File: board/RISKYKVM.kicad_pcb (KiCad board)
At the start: 4 copper layers, 24.9 x 35.6 mm, 19 parts, among them J1 DE9_Plug, J2 Conn_01x02, J3 USB_1, J4 Conn_01x08, U1 CH32V203C8T6, U2 LM1117MP-3.3

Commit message: v0.2
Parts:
- moved R3 2.02 mm to (119.8, 78.2), turned to 90 degrees
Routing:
- net +3.3V: track 50.5 -> 23.0 mm, vias 8 -> 7
- net GND: vias 12 -> 11
- added copper zone on In2.Cu, net +3.3V
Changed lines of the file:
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@@
     (fp_line (start 1 0.6) (end 1 -0.6)
       (stroke (width 0.1) (type solid)) (layer "F.Fab"))
-    (pad "1" smd roundrect (at -1.025 0 90) (size 1.15 1.4) (layers "F.Cu" "F.Paste" "F.Mask") (roundrect_rratio 0.217391)
+    (pad "1" smd roundrect (at -1.025 0 90) (size 1.15 1.4) (layers "F.Cu" "F.Paste" "F.Mask") (roundrect_rratio 0.2173913043)
       (net 44 "/LED1") (pinfunction "K") (pintype "passive"))
-    (pad "2" smd roundrect (at 1.025 0 90) (size 1.15 1.4) (layers "F.Cu" "F.Paste" "F.Mask") (roundrect_rratio 0.217391)
+    (pad "2" smd roundrect (at 1.025 0 90) (size 1.15 1.4) (layers "F.Cu" "F.Paste" "F.Mask") (roundrect_rratio 0.2173913043)
       (net 45 "Net-(D2-A)") (pinfunction "A") (pintype "passive"))
     (model "${KICAD6_3DMODEL_DIR}/LED_SMD.3dshapes/LED_0805_2012Metric.wrl"
@@
     (fp_line (start 1 0.6) (end 1 -0.6)
       (stroke (width 0.1) (type solid)) (layer "F.Fab"))
-    (pad "1" smd roundrect (at -1.025 0 90) (size 1.15 1.4) (layers "F.Cu" "F.Paste" "F.Mask") (roundrect_rratio 0.217391)
+    (pad "1" smd roundrect (at -1.025 0 90) (size 1.15 1.4) (layers "F.Cu" "F.Paste" "F.Mask") (roundrect_rratio 0.2173913043)
       (net 2 "GND") (pinfunction "K") (pintype "passive"))
-    (pad "2" smd roundrect (at 1.025 0 90) (size 1.15 1.4) (layers "F.Cu" "F.Paste" "F.Mask") (roundrect_rratio 0.217391)
+    (pad "2" smd roundrect (at 1.025 0 90) (size 1.15 1.4) (layers "F.Cu" "F.Paste" "F.Mask") (roundrect_rratio 0.2173913043)
       (net 18 "Net-(D1-A)") (pinfunction "A") (pintype "passive"))
     (model "${KICAD6_3DMODEL_DIR}/LED_SMD.3dshapes/LED_0805_2012Metric.wrl"
@@
   )
   (footprint "Resistor_SMD:R_0603_1608Metric_Pad0.98x0.95mm_HandSolder" (layer "B.Cu")
-    (at 119.8 80.27 -90)
+    (at 119.775 78.25 90)
     (descr "Resistor SMD 0603 (1608 Metric), square (rectangular) end terminal, IPC_7351 nominal with elongated pad for handsoldering. (Body size source: IPC-SM-782 page 72, https://www.pcb-3d.com/wordpress/wp-content/uploads/ipc-sm-782a_amendment_1_and_2.pdf), generated with kicad-footprint-generator")
     (tags "resistor handsolder")
@@
     (property "ki_keywords" "R res resistor")
     (attr smd)
-    (fp_text reference "R3" (at 2.93 -0.1 90) (layer "B.SilkS")
+    (fp_text reference "R3" (at -2.8 0.125 270) (layer "B.SilkS")
         (effects (font (size 1 1) (thickness 0.15)) (justify mirror))
     )
@@
     (fp_line (start 0.8 0.4125) (end 0.8 -0.4125)
       (stroke (width 0.1) (type solid)) (layer "B.Fab"))
-    (pad "1" smd roundrect (at -0.9125 0 270) (size 0.975 0.95) (layers "B.Cu" "B.Paste" "B.Mask") (roundrect_rratio 0.25)
+    (pad "1" smd roundrect (at -0.9125 0 90) (size 0.975 0.95) (layers "B.Cu" "B.Paste" "B.Mask") (roundrect_rratio 0.25)
       (net 45 "Net-(D2-A)") (pintype "passive"))
-    (pad "2" smd roundrect (at 0.9125 0 270) (size 0.975 0.95) (layers "B.Cu" "B.Paste" "B.Mask") (roundrect_rratio 0.25)
+    (pad "2" smd roundrect (at 0.9125 0 90) (size 0.975 0.95) (layers "B.Cu" "B.Paste" "B.Mask") (roundrect_rratio 0.25)
       (net 1 "+3.3V") (pintype "passive"))
     (model "${KICAD6_3DMODEL_DIR}/Resistor_SMD.3dshapes/R_0603_1608Metric.wrl"
@@
     (property "ki_keywords" "R res resistor")
     (attr smd)
-    (fp_text reference "R2" (at 0.0762 -1.27 270) (layer "B.SilkS")
+    (fp_text reference "R2" (at 0.1078 -1.7122 270) (layer "B.SilkS")
         (effects (font (size 1 1) (thickness 0.15)) (justify mirror))
     )
@@
     (effects (font (size 0.8128 0.8128) (thickness 0.1524) bold) (justify left bottom))
   )
-  (gr_text "POWER" (at 122.5 108.2 90) (layer "F.SilkS")
+  (gr_text "POWER" (at 123.15 108.125 90) (layer "F.SilkS")
     (effects (font (size 0.8128 0.8128) (thickness 0.1524) bold) (justify left bottom))
   )
@@
   (segment (start 125.596121 93.916221) (end 125.5861 93.9062) (width 0.127) (layer "F.Cu") (net 1))
   (segment (start 126.9986 90.0146) (end 126.9986 90.2364) (width 0.2) (layer "F.Cu") (net 1))
-  (segment (start 132.0854 95.4502) (end 132.4664 95.8312) (width 0.2) (layer "F.Cu") (net 1))
   (segment (start 132.4986 96.8187) (end 132.4997 96.8198) (width 0.127) (layer "F.Cu") (net 1))
   (segment (start 126.9986 88.4937) (end 126.9986 90.0146) (width 0.2) (layer "F.Cu") (net 1))
@@
   (segment (start 126.9986 90.2364) (end 127.107 90.3448) (width 0.2) (layer "F.Cu") (net 1))
   (segment (start 125.5861 89.9062) (end 126.8902 89.9062) (width 0.2) (layer "F.Cu") (net 1))
-  (segment (start 123.87 86.83) (end 123.87 86.82) (width 0.127) (layer "F.Cu") (net 1))
   (segment (start 133.9111 89.9062) (end 132.4986 89.9062) (width 0.2) (layer "F.Cu") (net 1))
   (segment (start 132.4664 96.7865) (end 132.4986 96.8187) (width 0.127) (layer "F.Cu") (net 1))
-  (segment (start 132.0854 90.3194) (end 127.1324 90.3194) (width 0.2) (layer "F.Cu") (net 1))
-  (segment (start 132.0854 90.3194) (end 132.0854 95.4502) (width 0.2) (layer "F.Cu") (net 1))
-  (segment (start 125.41 88.37) (end 123.87 86.83) (width 0.127) (layer "F.Cu") (net 1))
   (segment (start 132.4664 95.8312) (end 132.4664 96.7865) (width 0.127) (layer "F.Cu") (net 1))
-  (via (at 125.41 88.37) (size 0.6) (drill 0.3) (layers "F.Cu" "B.Cu") (net 1))
-  (via (at 123.87 86.82) (size 0.6) (drill 0.3) (layers "F.Cu" "B.Cu") (net 1))
   (via (at 122.63 98.74) (size 0.6) (drill 0.3) (layers "F.Cu" "B.Cu") (net 1))
   (via (at 132.0854 90.3194) (size 0.6) (drill 0.3) (layers "F.Cu" "B.Cu") (net 1))
+  (via (at 119.775 77.375) (size 0.6) (drill 0.3) (layers "F.Cu" "B.Cu") (net 1))
   (via (at 132.4664 95.8312) (size 0.6) (drill 0.3) (layers "F.Cu" "B.Cu") (net 1))
-  (via (at 122.63 100.1935) (size 0.6) (drill 0.3) (layers "F.Cu" "B.Cu") (net 1))
+  (via (at 121.925 104.65) (size 0.6) (drill 0.3) (layers "F.Cu" "B.Cu") (net 1))
   (via (at 127.107 90.3448) (size 0.6) (drill 0.3) (layers "F.Cu" "B.Cu") (net 1))
   (via (at 126.530218 93.916221) (size 0.6) (drill 0.3) (layers "F.Cu" "B.Cu") (net 1))
@@
   (segment (start 126.530218 94.264918) (end 126.530218 93.916221) (width 0.127) (layer "B.Cu") (net 1))
   (segment (start 127.5134 95.2481) (end 126.530218 94.264918) (width 0.127) (layer "B.Cu") (net 1))
-  (segment (start 121.905 103.955) (end 122.64 103.22) (width 0.127) (layer "B.Cu") (net 1))
   (segment (start 127.8222 95.5569) (end 131.7744 95.5569) (width 0.127) (layer "B.Cu") (net 1))
   (segment (start 122.5834 98.6934) (end 122.63 98.74) (width 0.127) (layer "B.Cu") (net 1))
   (segment (start 126.776139 93.6703) (end 126.530218 93.916221) (width 0.127) (layer "B.Cu") (net 1))
   (segment (start 132.4399 95.8047) (end 132.4664 95.8312) (width 0.2) (layer "B.Cu") (net 1))
-  (segment (start 121.905 104.72) (end 121.905 103.955) (width 0.127) (layer "B.Cu") (net 1))
   (segment (start 126.1219 95.2481) (end 122.63 98.74) (width 0.127) (layer "B.Cu") (net 1))
-  (segment (start 127.2097 90.1697) (end 125.41 88.37) (width 0.127) (layer "B.Cu") (net 1))
   (segment (start 127.4372 93.6703) (end 126.776139 93.6703) (width 0.127) (layer "B.Cu") (net 1))
-  (segment (start 122.64 100.2035) (end 122.63 100.1935) (width 0.127) (layer "B.Cu") (net 1))
   (segment (start 127.1589 90.3448) (end 127.2097 90.294) (width 0.2) (layer "B.Cu") (net 1))
-  (segment (start 122.64 103.22) (end 122.64 100.2035) (width 0.127) (layer "B.Cu") (net 1))
   (segment (start 127.5134 95.2481) (end 127.8222 95.5569) (width 0.127) (layer "B.Cu") (net 1))
   (segment (start 131.7744 95.5569) (end 132.4399 94.8914) (width 0.127) (layer "B.Cu") (net 1))
   (segment (start 127.107 90.3448) (end 127.1589 90.3448) (width 0.2) (layer "B.Cu") (net 1))
-  (segment (start 123.87 85.2525) (end 119.8 81.1825) (width 0.127) (layer "B.Cu") (net 1))
-  (segment (start 123.87 86.82) (end 123.87 85.2525) (width 0.127) (layer "B.Cu") (net 1))
   (segment (start 127.5134 95.2481) (end 126.1219 95.2481) (width 0.127) (layer "B.Cu") (net 1))
   (segment (start 127.2097 90.294) (end 127.2097 90.1697) (width 0.127) (layer "B.Cu") (net 1))
@@
   (via (at 129.72 77.77) (size 0.6) (drill 0.3) (layers "F.Cu" "B.Cu") (free) (net 2))
   (via (at 128.01 99.54) (size 0.6) (drill 0.3) (layers "F.Cu" "B.Cu") (free) (net 2))
-  (via (at 121.95 85.32) (size 0.6) (drill 0.3) (layers "F.Cu" "B.Cu") (free) (net 2))
   (via (at 127.5 87.39) (size 0.6) (drill 0.3) (layers "F.Cu" "B.Cu") (net 2))
   (via (at 122.6 97) (size 0.6) (drill 0.3) (layers "F.Cu" "B.Cu") (net 2))
@@
       )
     )
+  )
+  (zone (net 1) (net_name "+3.3V") (layer "In2.Cu") (hatch edge 0.5)
+    (priority 4)
+    (connect_pads (clearance 0.5))
+    (min_thickness 0.25) (filled_areas_thickness no)
+    (fill yes (thermal_gap 0.5) (thermal_bridge_width 0.5))
+    (polygon
+      (pts
+        (xy 142.9 74.85)
+        (xy 142.9 110.35)
+        (xy 118.025 110.35)
+        (xy 118 74.85)
+      )
+    )

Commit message: Fix issues related to BOOT0 and BOOT1
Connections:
- U1 pad 20: /PIN5 -> GND
- U1 pad 21: /PIN9 -> /PIN5
- U1 pad 22: /PIN4 -> /PIN9
- U1 pad 25: /PIN3 -> /PIN4
- U1 pad 26: /PIN2 -> /PIN3
- U1 pad 27: /PIN6 -> /PIN2
- U1 pad 28: /PIN1 -> /PIN6
- U1 pad 29: unconnected-(U1-PA8(FT)-Pad29) -> /PIN1
- U1 pad 44: unconnected-(U1-BOOT0-Pad44) -> GND
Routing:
- net GND: track 16.6 -> 21.4 mm, vias 11 -> 10
- net /PIN4: track 12.6 -> 15.3 mm
- net /PIN3: track 13.9 -> 15.9 mm
- net /PIN5: track 13.4 -> 14.4 mm
- net /PIN2: track 14.4 -> 15.5 mm
- net /PIN6: track 14.7 -> 15.6 mm
- net /PIN1: track 15.1 -> 15.9 mm
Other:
- board text added: "5V"
- board text added: "CL"
- board text added: "DT"
- board text added: "G"
- board text added: "PWR"
- board text added: "R"
- board text added: "RDY"
- board text removed: "POWER"
- board text removed: "READY"

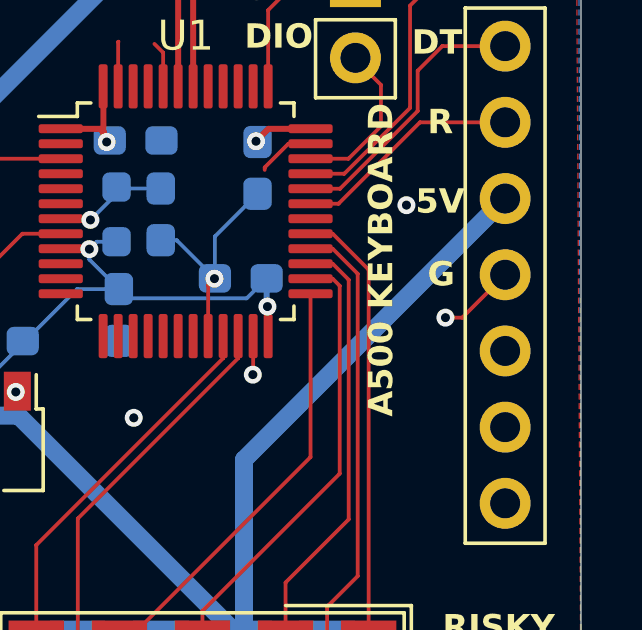
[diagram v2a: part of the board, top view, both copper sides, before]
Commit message: KEY in Amiga Port missing
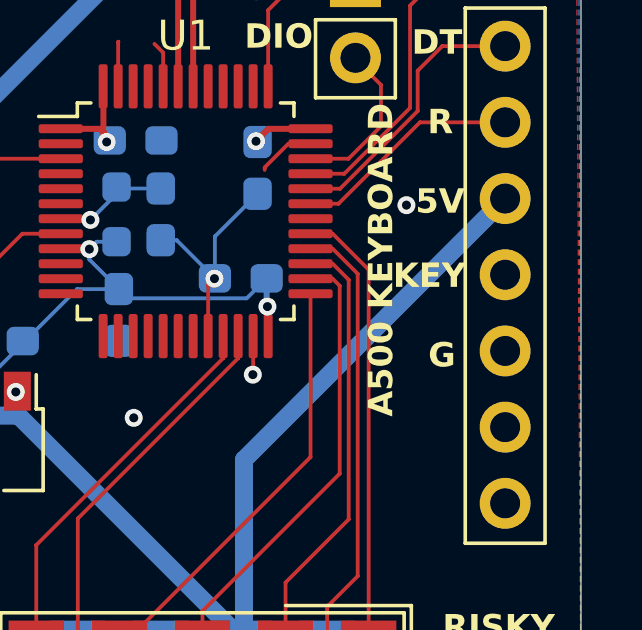
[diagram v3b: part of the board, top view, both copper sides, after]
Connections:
- J4 pad 5: GND -> unconnected-(J4-Pin_5-Pad5)
- J4 pad 6: unconnected-(J4-Pin_6-Pad6) -> GND
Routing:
- net GND: track 21.4 -> 18.8 mm, vias 10 -> 9
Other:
- board text added: "KEY"
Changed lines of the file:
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@@
   (net 21 "unconnected-(U1-PB0_ADC8-Pad18)")
   (net 22 "unconnected-(U1-PB1_ADC9-Pad19)")
-  (net 23 "/KB_CLK")
-  (net 24 "/KB_DATA")
-  (net 25 "/KB_RESET")
-  (net 26 "unconnected-(J4-Pin_6-Pad6)")
+  (net 23 "unconnected-(J4-Pin_5-Pad5)")
+  (net 24 "/KB_CLK")
+  (net 25 "/KB_DATA")
+  (net 26 "/KB_RESET")
   (net 27 "unconnected-(J4-Pin_7-Pad7)")
   (net 28 "unconnected-(J4-Pin_8-Pad8)")
@@
       (stroke (width 0.1) (type solid)) (layer "F.Fab"))
     (pad "1" thru_hole rect (at 0 0) (size 1.7 1.7) (drill 1) (layers "*.Cu" "*.Mask")
-      (net 23 "/KB_CLK") (pinfunction "Pin_1") (pintype "passive"))
+      (net 24 "/KB_CLK") (pinfunction "Pin_1") (pintype "passive"))
     (pad "2" thru_hole oval (at 0 2.54) (size 1.7 1.7) (drill 1) (layers "*.Cu" "*.Mask")
-      (net 24 "/KB_DATA") (pinfunction "Pin_2") (pintype "passive"))
+      (net 25 "/KB_DATA") (pinfunction "Pin_2") (pintype "passive"))
     (pad "3" thru_hole oval (at 0 5.08) (size 1.7 1.7) (drill 1) (layers "*.Cu" "*.Mask")
-      (net 25 "/KB_RESET") (pinfunction "Pin_3") (pintype "passive"))
+      (net 26 "/KB_RESET") (pinfunction "Pin_3") (pintype "passive"))
     (pad "4" thru_hole oval (at 0 7.62) (size 1.7 1.7) (drill 1) (layers "*.Cu" "*.Mask")
       (net 3 "+5V") (pinfunction "Pin_4") (pintype "passive"))
     (pad "5" thru_hole oval (at 0 10.16) (size 1.7 1.7) (drill 1) (layers "*.Cu" "*.Mask")
-      (net 2 "GND") (pinfunction "Pin_5") (pintype "passive"))
+      (net 23 "unconnected-(J4-Pin_5-Pad5)") (pinfunction "Pin_5") (pintype "passive+no_connect"))
     (pad "6" thru_hole oval (at 0 12.7) (size 1.7 1.7) (drill 1) (layers "*.Cu" "*.Mask")
-      (net 26 "unconnected-(J4-Pin_6-Pad6)") (pinfunction "Pin_6") (pintype "passive+no_connect"))
+      (net 2 "GND") (pinfunction "Pin_6") (pintype "passive"))
     (pad "7" thru_hole oval (at 0 15.24) (size 1.7 1.7) (drill 1) (layers "*.Cu" "*.Mask")
       (net 27 "unconnected-(J4-Pin_7-Pad7)") (pinfunction "Pin_7") (pintype "passive+no_connect"))
@@
       (net 38 "unconnected-(U1-PA9(FT)-Pad30)") (pinfunction "PA9(FT)") (pintype "bidirectional+no_connect"))
     (pad "31" smd roundrect (at 4.1625 -0.25) (size 1.475 0.3) (layers "F.Cu" "F.Paste" "F.Mask") (roundrect_rratio 0.25)
-      (net 25 "/KB_RESET") (pinfunction "PA10(FT)") (pintype "bidirectional"))
+      (net 26 "/KB_RESET") (pinfunction "PA10(FT)") (pintype "bidirectional"))
     (pad "32" smd roundrect (at 4.1625 -0.75) (size 1.475 0.3) (layers "F.Cu" "F.Paste" "F.Mask") (roundrect_rratio 0.25)
-      (net 24 "/KB_DATA") (pinfunction "PA11_USB1DM(FT)") (pintype "bidirectional"))
+      (net 25 "/KB_DATA") (pinfunction "PA11_USB1DM(FT)") (pintype "bidirectional"))
     (pad "33" smd roundrect (at 4.1625 -1.25) (size 1.475 0.3) (layers "F.Cu" "F.Paste" "F.Mask") (roundrect_rratio 0.25)
-      (net 23 "/KB_CLK") (pinfunction "PA12_USB1DP(FT)") (pintype "bidirectional"))
+      (net 24 "/KB_CLK") (pinfunction "PA12_USB1DP(FT)") (pintype "bidirectional"))
     (pad "34" smd roundrect (at 4.1625 -1.75) (size 1.475 0.3) (layers "F.Cu" "F.Paste" "F.Mask") (roundrect_rratio 0.25)
       (net 13 "/SWDIO") (pinfunction "PA13_SWDIO(FT)") (pintype "bidirectional"))
@@
     (effects (font (size 0.8128 0.8128) (thickness 0.1524) bold) (justify left bottom))
   )
-  (gr_text "G" (at 137.8 95.225) (layer "F.SilkS")
+  (gr_text "G" (at 137.825 97.925) (layer "F.SilkS")
     (effects (font (size 0.8128 0.8128) (thickness 0.1524) bold) (justify left bottom))
   )
@@
   )
   (gr_text "5V" (at 137.4 92.8) (layer "F.SilkS")
+    (effects (font (size 0.8128 0.8128) (thickness 0.1524) bold) (justify left bottom))
+  )
+  (gr_text "KEY" (at 136.65 95.275) (layer "F.SilkS")
     (effects (font (size 0.8128 0.8128) (thickness 0.1524) bold) (justify left bottom))
   )
@@
   (segment (start 130.49 95.11) (end 130.7 94.9) (width 0.127) (layer "F.Cu") (net 2))
   (segment (start 132.375 91.192501) (end 132.375 91.275) (width 0.127) (layer "F.Cu") (net 2))
-  (segment (start 138.96 96.2) (end 140.39 94.77) (width 0.127) (layer "F.Cu") (net 2))
-  (segment (start 138.4 96.2) (end 138.96 96.2) (width 0.127) (layer "F.Cu") (net 2))
   (segment (start 130.49 96.815) (end 130.49 95.11) (width 0.127) (layer "F.Cu") (net 2))
   (segment (start 127.49 87.01) (end 127.5 87) (width 0.127) (layer "F.Cu") (net 2))
@@
   (via (at 137.1 92.45) (size 0.6) (drill 0.3) (layers "F.Cu" "B.Cu") (free) (net 2))
   (via (at 128.9 108.1) (size 0.6) (drill 0.3) (layers "F.Cu" "B.Cu") (net 2))
-  (via (at 138.4 96.2) (size 0.6) (drill 0.3) (layers "F.Cu" "B.Cu") (free) (net 2))
   (via (at 131.98 98.1) (size 0.6) (drill 0.3) (layers "F.Cu" "B.Cu") (net 2))
   (via (at 124.0778 98.6769) (size 0.6) (drill 0.3) (layers "F.Cu" "B.Cu") (net 2))
@@
   (segment (start 129.5186 81.6107) (end 129.175 81.2671) (width 0.2) (layer "F.Cu") (net 16))
   (via (at 120.15 104.63) (size 0.6) (drill 0.3) (layers "F.Cu" "B.Cu") (net 18))
-  (segment (start 133.9025 91.4025) (end 135.026982 91.4025) (width 0.127) (layer "F.Cu") (net 23))
-  (segment (start 135.026982 91.4025) (end 137.22 89.209482) (width 0.127) (layer "F.Cu") (net 23))
-  (segment (start 138.41 84.61) (end 140.39 84.61) (width 0.127) (layer "F.Cu") (net 23))
-  (segment (start 137.22 85.8) (end 138.41 84.61) (width 0.127) (layer "F.Cu") (net 23))
-  (segment (start 137.22 89.209482) (end 137.22 85.8) (width 0.127) (layer "F.Cu") (net 23))
-  (segment (start 138.294 87.15) (end 140.39 87.15) (width 0.127) (layer "F.Cu") (net 24))
-  (segment (start 137.474 87.97) (end 138.294 87.15) (width 0.127) (layer "F.Cu") (net 24))
-  (segment (start 133.9025 91.9025) (end 134.886192 91.9025) (width 0.127) (layer "F.Cu") (net 24))
-  (segment (start 134.886192 91.9025) (end 137.474 89.314692) (width 0.127) (layer "F.Cu") (net 24))
-  (segment (start 137.474 89.314692) (end 137.474 87.97) (width 0.127) (layer "F.Cu") (net 24))
-  (segment (start 133.9025 92.4025) (end 134.8375 92.4025) (width 0.127) (layer "F.Cu") (net 25))
-  (segment (start 134.8375 92.4025) (end 137.55 89.69) (width 0.127) (layer "F.Cu") (net 25))
-  (segment (start 137.55 89.69) (end 140.39 89.69) (width 0.127) (layer "F.Cu") (net 25))
+  (segment (start 133.9025 91.4025) (end 135.026982 91.4025) (width 0.127) (layer "F.Cu") (net 24))
+  (segment (start 135.026982 91.4025) (end 137.22 89.209482) (width 0.127) (layer "F.Cu") (net 24))
+  (segment (start 138.41 84.61) (end 140.39 84.61) (width 0.127) (layer "F.Cu") (net 24))
+  (segment (start 137.22 85.8) (end 138.41 84.61) (width 0.127) (layer "F.Cu") (net 24))
+  (segment (start 137.22 89.209482) (end 137.22 85.8) (width 0.127) (layer "F.Cu") (net 24))
+  (segment (start 138.294 87.15) (end 140.39 87.15) (width 0.127) (layer "F.Cu") (net 25))
+  (segment (start 137.474 87.97) (end 138.294 87.15) (width 0.127) (layer "F.Cu") (net 25))
+  (segment (start 133.9025 91.9025) (end 134.886192 91.9025) (width 0.127) (layer "F.Cu") (net 25))
+  (segment (start 134.886192 91.9025) (end 137.474 89.314692) (width 0.127) (layer "F.Cu") (net 25))
+  (segment (start 137.474 89.314692) (end 137.474 87.97) (width 0.127) (layer "F.Cu") (net 25))
+  (segment (start 133.9025 92.4025) (end 134.8375 92.4025) (width 0.127) (layer "F.Cu") (net 26))
+  (segment (start 134.8375 92.4025) (end 137.55 89.69) (width 0.127) (layer "F.Cu") (net 26))
+  (segment (start 137.55 89.69) (end 140.39 89.69) (width 0.127) (layer "F.Cu") (net 26))
   (segment (start 125.5265 91.9658) (end 125.5861 91.9062) (width 0.127) (layer "F.Cu") (net 29))
   (segment (start 125.583 95.4093) (end 125.5861 95.4062) (width 0.2) (layer "F.Cu") (net 32))
